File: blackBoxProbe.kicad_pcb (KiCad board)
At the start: 4 copper layers, 44 x 44 mm, 80 parts, among them J1 USB-ID, J2 JTAG_2X05, J3 JTAG_2X05, J4 Conn_01x04, Q1 Q_NMOS_DUAL, Q2 Q_PMOS_DUAL, U1 MCP1702-MB, U2 USBLC6-2, U3 STM32F103CBT, U4 74X2T45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

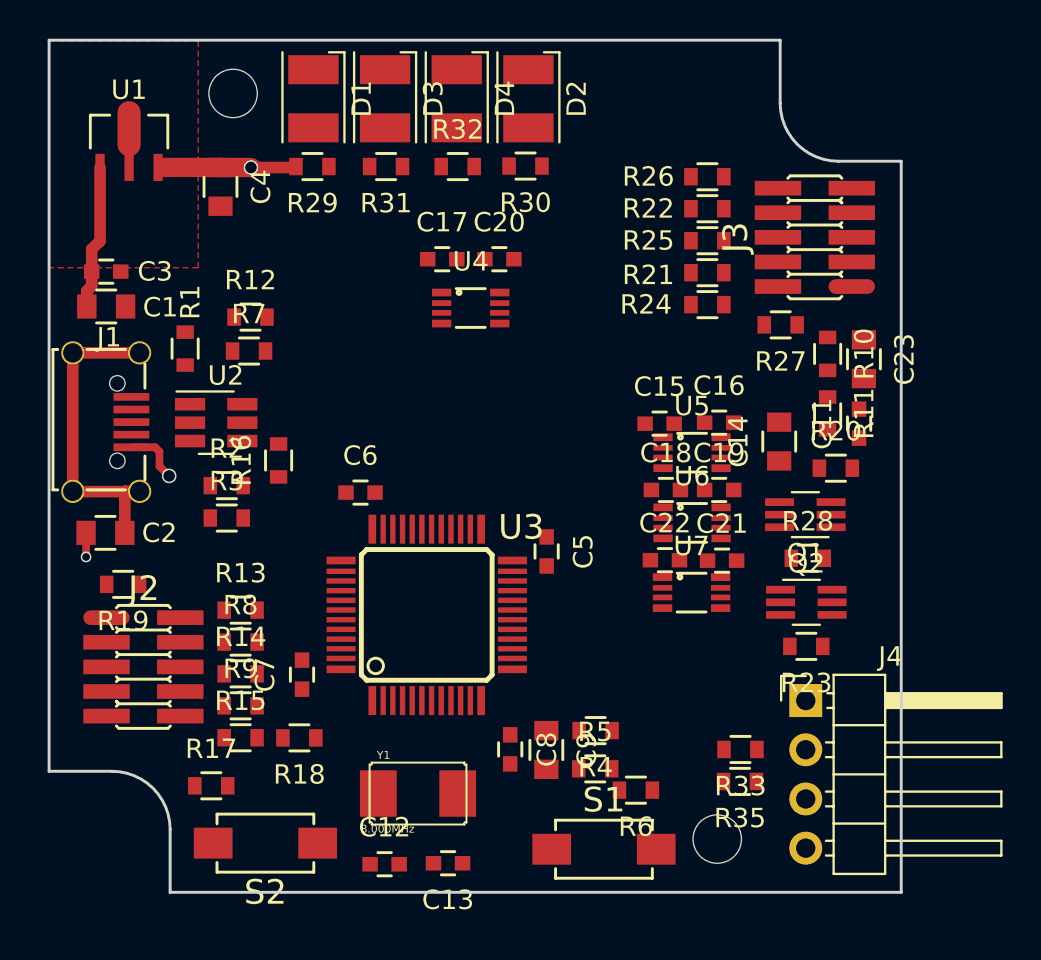
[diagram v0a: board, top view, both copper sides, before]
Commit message: DONE: tuned USB differential pair length WIP: inital layouting WIP: further optimal placing
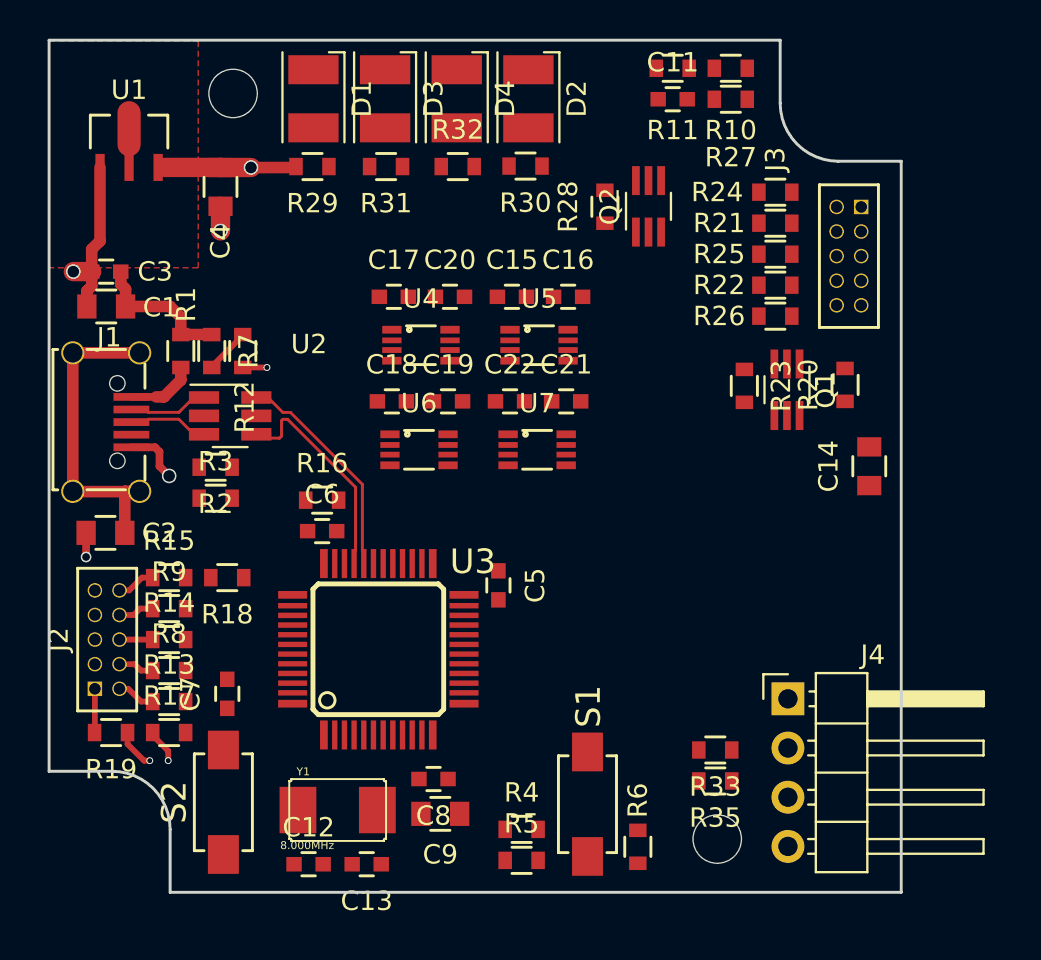
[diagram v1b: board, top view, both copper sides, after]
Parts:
- removed C23: 10u, SquantorRcl:C_0805
- J2, J3: footprint SquantorConnectors:Header-0127-2X05-SMD -> SquantorConnectors:Header-0127-2X5-H006
- R17: value 10K -> 1K
- moved Q2 22.0 mm to (45.2, 159.8), turned to 90 degrees
- moved R28 21.0 mm to (43.0, 159.8), turned to 90 degrees
- moved R11 19.5 mm to (46.5, 152.7), turned to 180 degrees
- moved C11 19.3 mm to (46.5, 154.3), turned to 0 degrees
- moved R10 15.6 mm to (49.5, 152.7), turned to 180 degrees
- moved C18 14.9 mm to (32.0, 169.9)
- moved C19 14.7 mm to (34.9, 169.9)
- moved U6 14.6 mm to (33.4, 172.4)
- moved R23 13.8 mm to (50.2, 169.1), turned to 270 degrees
- moved R27 11.9 mm to (49.5, 154.3)
- moved C21 11.5 mm to (41.0, 169.9)
- moved C22 11.5 mm to (38.1, 169.9)
- moved U7 10.9 mm to (39.5, 172.4)
- moved C16 10.2 mm to (41.1, 164.5)
- moved C15 10.1 mm to (38.2, 164.5)
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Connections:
- net Net-(J1-Pad2) renamed /USB_D_C-
- net Net-(J1-Pad3) renamed /USB_D_C+
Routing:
- net /USB_D+: track 0.00 -> 12.7 mm
- net /USB_D-: track 0.00 -> 11.9 mm
- net +5V: track 0.00 -> 7.48 mm
- net GND: track 11.7 -> 17.0 mm, vias 2 -> 6
- net /USB_D_C+: track 0.00 -> 4.13 mm
- net /USB_D_C-: track 0.00 -> 4.13 mm
- net Net-(J1-Pad1): track 0.00 -> 3.56 mm
- net /USB_V: track 0.00 -> 2.36 mm
- net Net-(J2-Pad1): track 0.00 -> 2.27 mm
- net +3V3: track 7.14 -> 9.24 mm, vias 1 -> 2
- net Net-(J2-Pad2): track 0.00 -> 1.99 mm
- net Net-(J2-Pad10): track 0.00 -> 1.99 mm
- net Net-(J2-Pad8): track 0.00 -> 1.85 mm
- net Net-(J2-Pad4): track 0.00 -> 1.85 mm
- net Net-(J2-Pad6): track 0.00 -> 1.71 mm

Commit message: WIP: More routing DONE: optimization of components, removing redudant/superflous components WIP: more optimal placement, maybe I can fit this in a 44 by 30mm box?
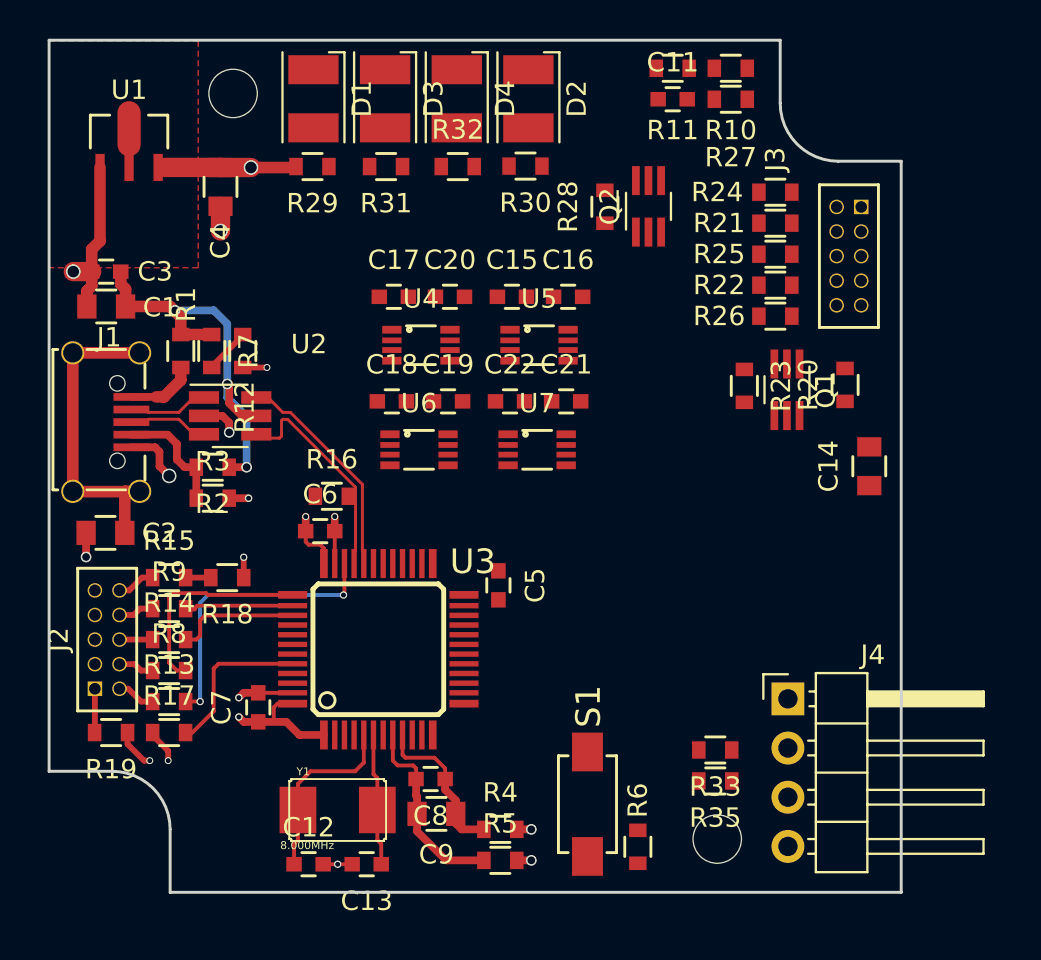
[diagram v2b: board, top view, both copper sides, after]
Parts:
- removed S2: 2pin_tact_switch, SquantorButtons:DTSM3
- moved C7 1.75 mm to (25.1, 185.7)
- moved R4 1.10 mm to (37.6, 192.0)
- moved R5 1.10 mm to (37.6, 193.6)
- moved R16 0.54 mm to (28.9, 174.8)
- moved C9 0.20 mm to (34.3, 191.2)
- moved C8 0.15 mm to (34.0, 189.4)
- moved R2 0.15 mm to (22.8, 173.3)
- moved R3 0.15 mm to (22.8, 174.9)
- moved C6 0.10 mm to (28.3, 176.6)
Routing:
- net /MCU_TMS: track 0.00 -> 15.1 mm, vias 0 -> 2
- net +5V: track 7.48 -> 22.0 mm, vias 0 -> 3
- net +3V3: track 9.24 -> 21.5 mm, vias 2 -> 6
- net /MCU_TCK: track 0.00 -> 10.9 mm
- net GND: track 17.0 -> 27.7 mm, vias 6 -> 12
- net GNDA: track 0.00 -> 10.0 mm
- net Net-(C12-Pad1): track 0.00 -> 9.51 mm
- net Net-(R17-Pad2): track 0.00 -> 8.28 mm
- net VDDA: track 0.00 -> 8.17 mm
- net Net-(C13-Pad1): track 0.00 -> 6.84 mm
- net /MCU_TDO: track 0.00 -> 6.51 mm
- net Net-(J1-Pad4): track 0.00 -> 6.11 mm
- net /MCU_TDI: track 0.00 -> 5.59 mm
- net /MCU_RST: track 0.00 -> 1.30 mm

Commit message: WIP: Futher layout, done power switch, reset circuit
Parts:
- moved C11 21.4 mm to (55.6, 173.6)
- moved R11 21.3 mm to (55.6, 172.0)
- moved R28 20.7 mm to (53.4, 177.8), turned to 270 degrees
- moved Q2 20.0 mm to (55.7, 176.9)
- moved R10 18.7 mm to (55.6, 170.4)
- moved R27 15.7 mm to (55.6, 168.8)
- moved C14 12.2 mm to (46.7, 180.3)
- moved D2 7.45 mm to (31.6, 154.3)
- moved R30 7.35 mm to (31.6, 157.6)
- moved R20 6.05 mm to (49.4, 168.3)
- moved C18 3.70 mm to (35.7, 169.9)
- moved C19 3.70 mm to (38.6, 169.9)
- moved C20 3.70 mm to (38.7, 164.5)
- moved C21 3.70 mm to (44.7, 169.9)
- moved U4 3.70 mm to (37.2, 167.0)
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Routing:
- net /LED2: track 0.00 -> 36.7 mm, vias 0 -> 2
- net /LED1: track 0.00 -> 36.2 mm, vias 0 -> 2
- net /LED0: track 0.00 -> 35.7 mm, vias 0 -> 2
- net /PROBE_VDD: track 0.00 -> 35.3 mm
- net /PROBE_I_RST: track 0.00 -> 26.7 mm, vias 0 -> 2
- net /USB_V: track 2.36 -> 29.0 mm, vias 0 -> 2
- net /BUTTON: track 0.00 -> 25.3 mm
- net /MCU_RST: track 1.30 -> 22.9 mm, vias 0 -> 2
- net /USB_PU: track 0.00 -> 12.6 mm, vias 0 -> 2
- net +3V3: track 21.5 -> 32.7 mm, vias 6 -> 10
- net GND: track 27.7 -> 37.3 mm, vias 12 -> 14
- net +5V: track 22.0 -> 29.5 mm
- net Net-(J3-Pad2): track 0.00 -> 3.49 mm
- net Net-(J3-Pad10): track 0.00 -> 3.49 mm
- net Net-(J3-Pad8): track 0.00 -> 3.35 mm
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
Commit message: WIP: additional routing WIP: placed the level shifting network WIP: Further component optimization and removal
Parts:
- removed R27: 100, SquantorRcl:R_0603_hand
- moved C20 12.7 mm to (47.0, 174.1), turned to 180 degrees
- moved U4 12.7 mm to (45.5, 176.6)
- moved C17 12.6 mm to (44.0, 174.1)
- moved C22 12.0 mm to (47.1, 159.1), turned to 180 degrees
- moved C18 11.3 mm to (47.0, 169.1), turned to 180 degrees
- moved U7 11.1 mm to (45.6, 161.6)
- moved C21 10.8 mm to (44.1, 159.1)
- moved U6 8.44 mm to (45.5, 171.6)
- moved C14 6.85 mm to (53.5, 181.1), turned to 180 degrees
- moved R20 6.22 mm to (55.6, 168.8), turned to 180 degrees
- moved C19 5.46 mm to (44.0, 169.1)
- moved C16 2.24 mm to (47.0, 164.1), turned to 180 degrees
- moved U5 2.24 mm to (45.5, 166.6)
- moved C15 2.14 mm to (44.0, 164.1)
- moved R33 0.10 mm to (48.7, 187.8)
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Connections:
- R20 pad 1: /PROBE_E_VDD -> /PROBE_VDD
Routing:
- net GND: track 37.3 -> 82.1 mm, vias 14 -> 26
- net /PROBE_VDD: track 35.3 -> 74.9 mm, vias 0 -> 4
- net /PROBE_E_RX: track 0.00 -> 20.9 mm
- net +3V3: track 32.7 -> 48.5 mm, vias 10 -> 18
- net /PROBE_E_TX: track 0.00 -> 13.4 mm
- net /PROBE_E_TDO: track 0.00 -> 11.4 mm, vias 0 -> 2
- net /PROBE_E_RST: track 0.00 -> 10.1 mm
- net Net-(Q2-Pad1): track 0.00 -> 8.30 mm
- net /PROBE_E_TCK: track 0.00 -> 7.81 mm
- net /TARGET_PWR_EN: track 0.00 -> 6.87 mm
- net /PROBE_E_TDI: track 0.00 -> 4.99 mm
- net /PROBE_E_TMS: track 0.00 -> 4.87 mm
- net Net-(J4-Pad3): track 0.00 -> 3.29 mm
- net /TARGET_PWR_SENSE: track 0.00 -> 3.26 mm
- net Net-(J4-Pad2): track 0.00 -> 2.90 mm

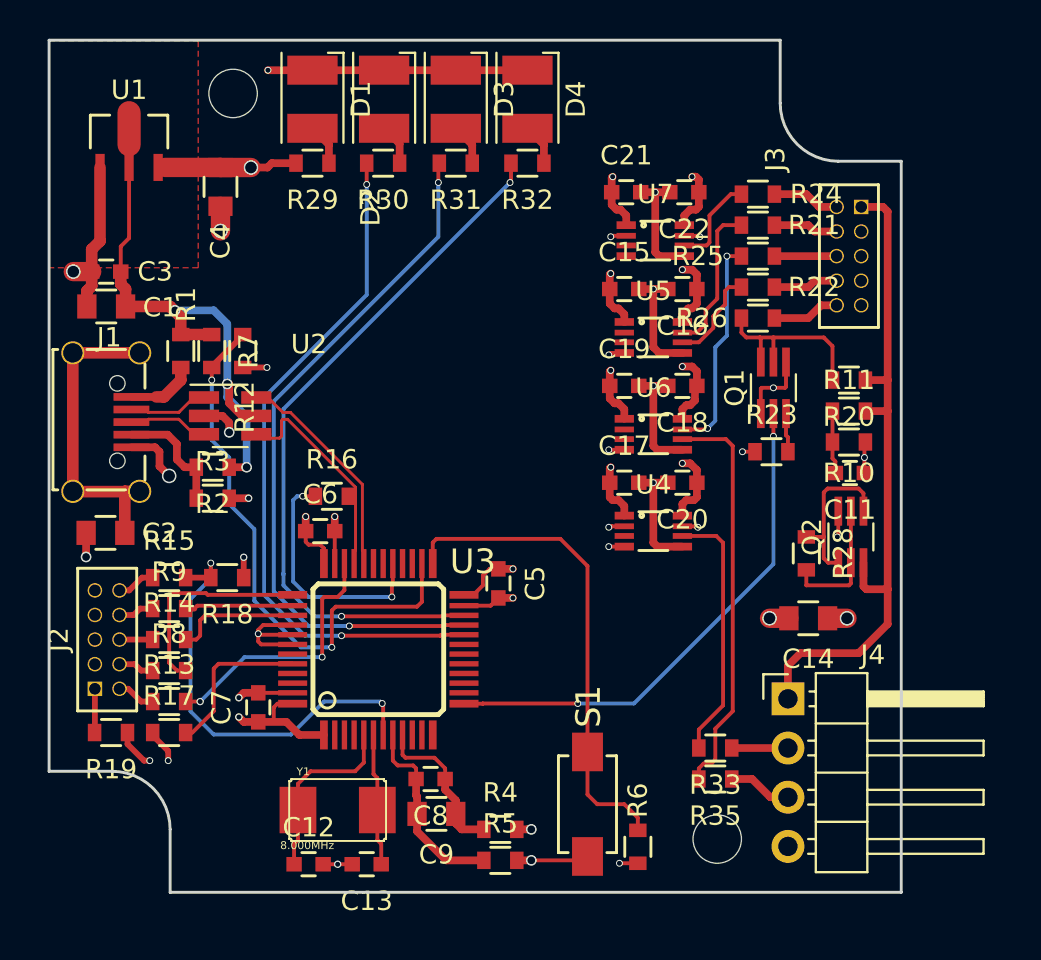
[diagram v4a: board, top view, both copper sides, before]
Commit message: DONE: routing of all nets, visual check still needed
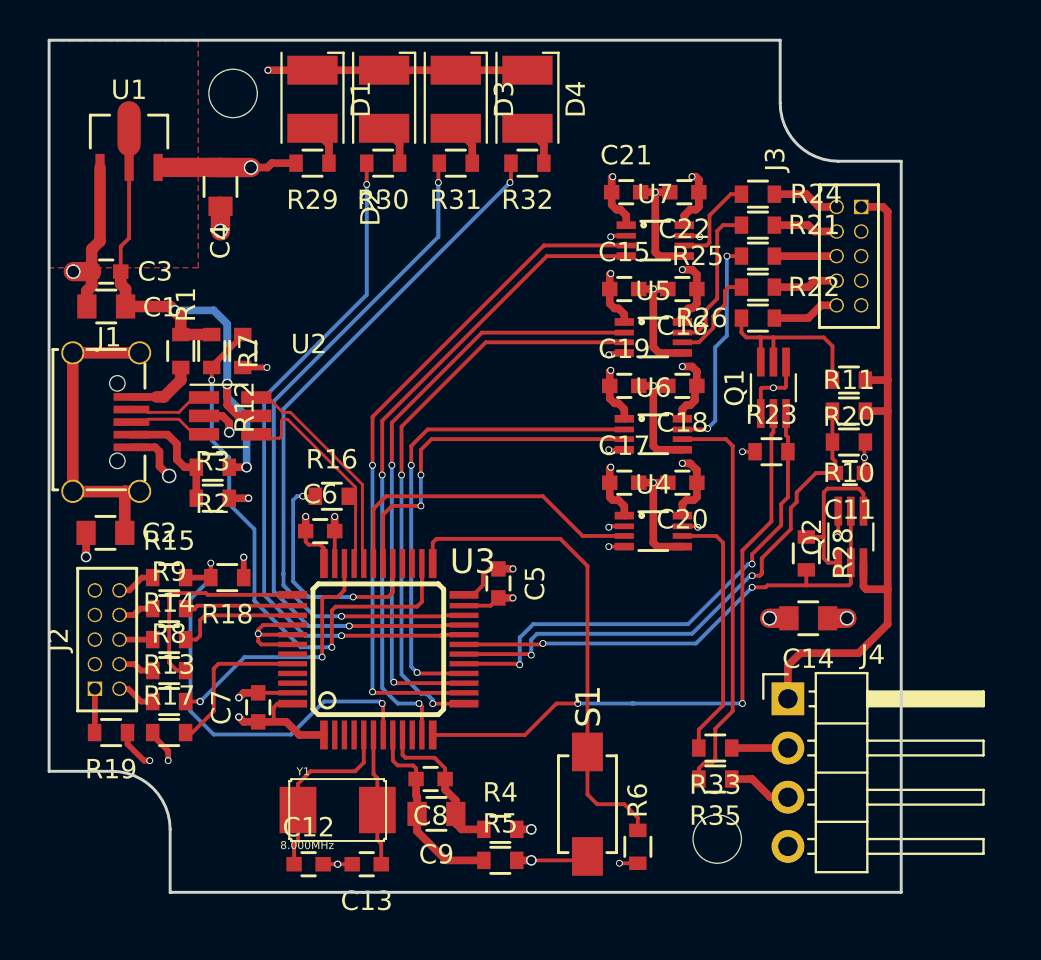
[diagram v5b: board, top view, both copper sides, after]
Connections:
- U3 pad 12: (no net) -> /PROBE_I_RST
- U3 pad 13: /PROBE_I_RST -> /PROBE_I_TDI
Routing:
- net /PROBE_I_TMS: track 0.00 -> 35.7 mm, vias 0 -> 2
- net /PROBE_TMS_DIR: track 0.00 -> 33.8 mm, vias 0 -> 2
- net /PROBE_I_TCK: track 0.00 -> 31.0 mm, vias 0 -> 2
- net /PROBE_I_TDI: track 0.00 -> 30.1 mm, vias 0 -> 2
- net /PROBE_I_TDO: track 0.00 -> 25.6 mm, vias 0 -> 2
- net /TARGET_PWR_SENSE: track 3.26 -> 28.2 mm, vias 0 -> 2
- net /PROBE_I_RST_SEN: track 2.01 -> 26.4 mm, vias 0 -> 2
- net /TARGET_PWR_EN: track 6.87 -> 25.8 mm, vias 0 -> 2
- net /PROBE_I_RX: track 0.00 -> 18.3 mm, vias 0 -> 2
- net /PROBE_I_TX: track 0.00 -> 16.9 mm
- net /PROBE_I_RST: track 26.7 -> 32.4 mm

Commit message: FIX: incorrect pin mapping of STM32 DONE: changed to 3mm leds, plenty of space DONE: routing WIP: Silk/value placing
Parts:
- D1, D2, D3, D4: footprint LEDs:LED_PLCC-2 -> LEDs:LED_D3.0mm
- moved D4 10.6 mm to (49.5, 153.0)
- moved D3 9.24 mm to (44.5, 153.0)
- moved D2 7.87 mm to (39.4, 153.0)
- moved D1 6.51 mm to (34.3, 153.0)
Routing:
- net GND: track 82.1 -> 68.7 mm, vias 26 -> 25

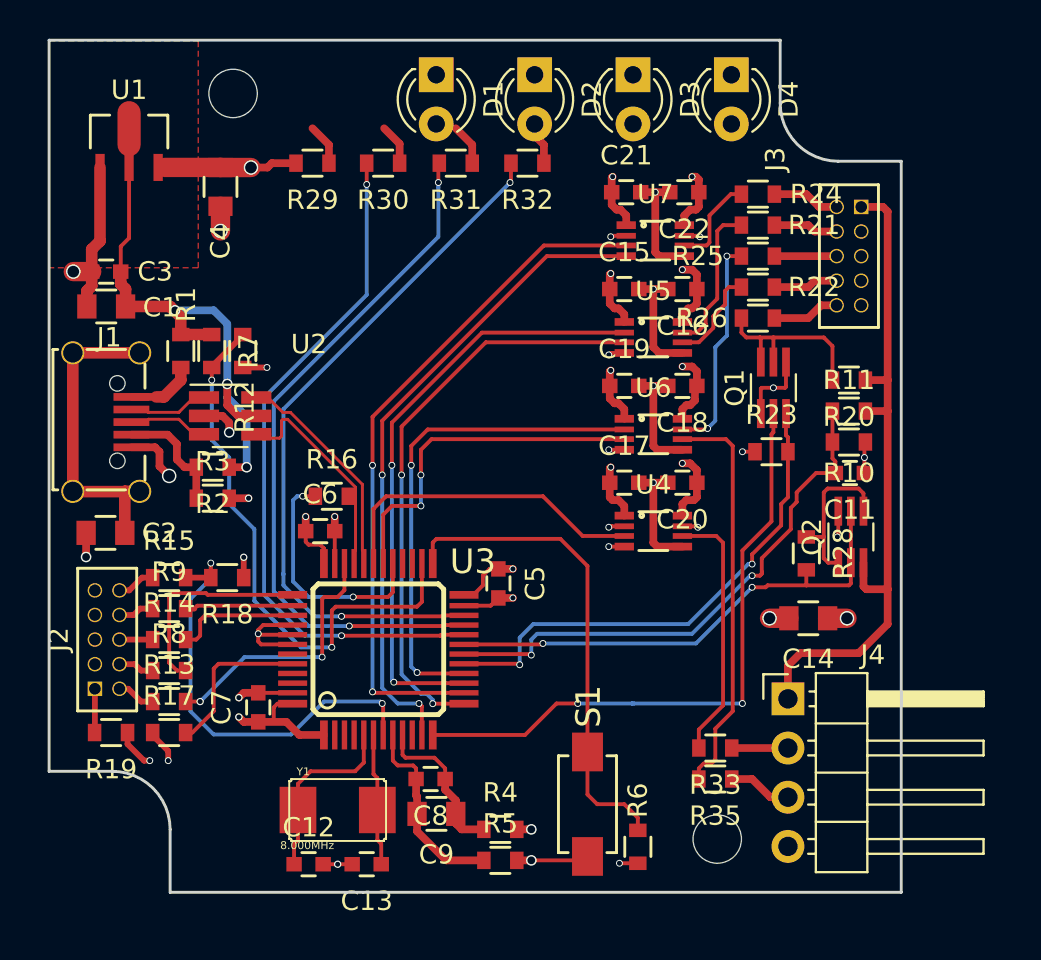
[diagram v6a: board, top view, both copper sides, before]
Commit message: DONE: placed all the silkscreen designations
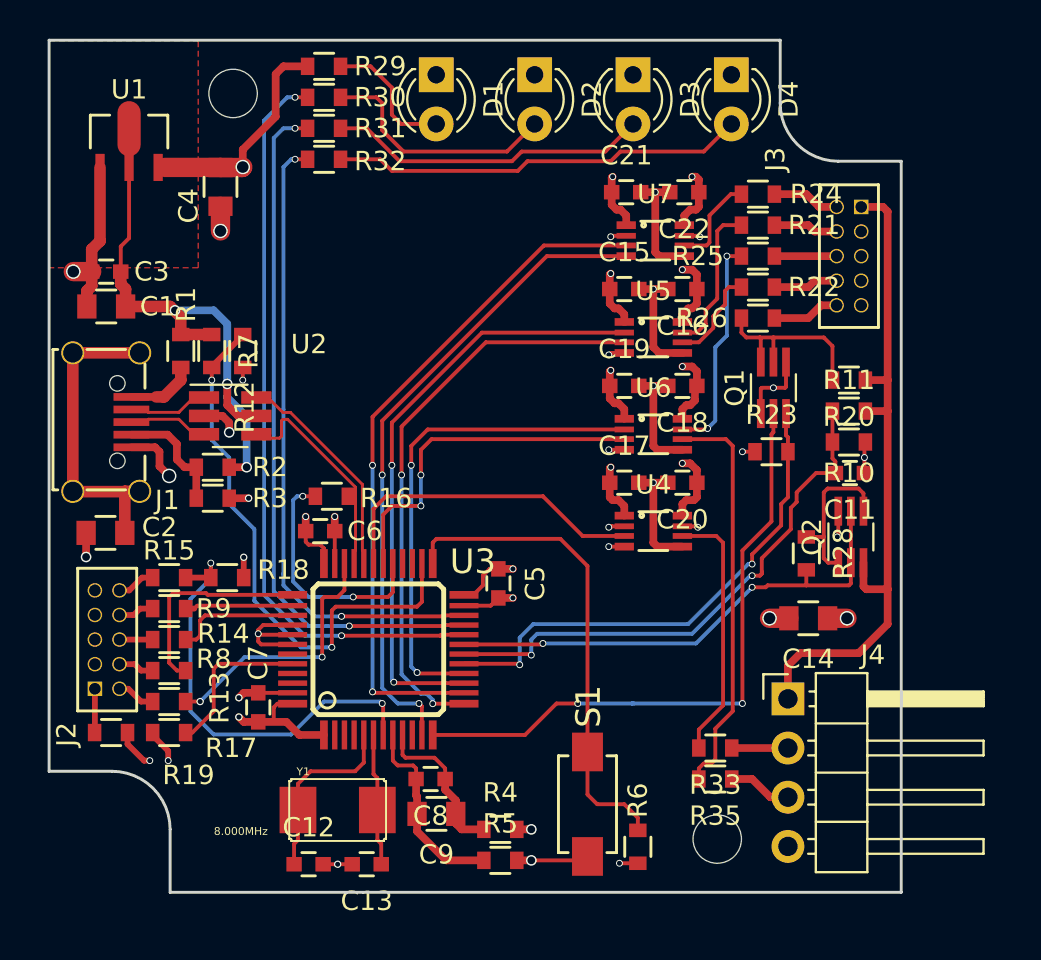
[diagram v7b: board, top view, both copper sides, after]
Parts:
- moved R32 10.5 mm to (28.5, 157.4)
- moved R31 7.03 mm to (28.5, 155.8)
- moved R29 5.04 mm to (28.5, 152.6)
- moved R30 4.57 mm to (28.5, 154.2)
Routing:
- net Net-(D4-Pad2): track 2.15 -> 21.4 mm
- net Net-(D3-Pad2): track 2.15 -> 16.6 mm
- net Net-(D2-Pad2): track 2.13 -> 12.6 mm
- net Net-(D1-Pad2): track 2.15 -> 6.99 mm
- net +3V3: track 48.5 -> 53.0 mm
- net /LED2: track 36.7 -> 33.1 mm
- net /LED0: track 35.7 -> 38.5 mm
- net GND: track 68.7 -> 68.1 mm
